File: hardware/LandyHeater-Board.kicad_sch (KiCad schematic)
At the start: 0 parts

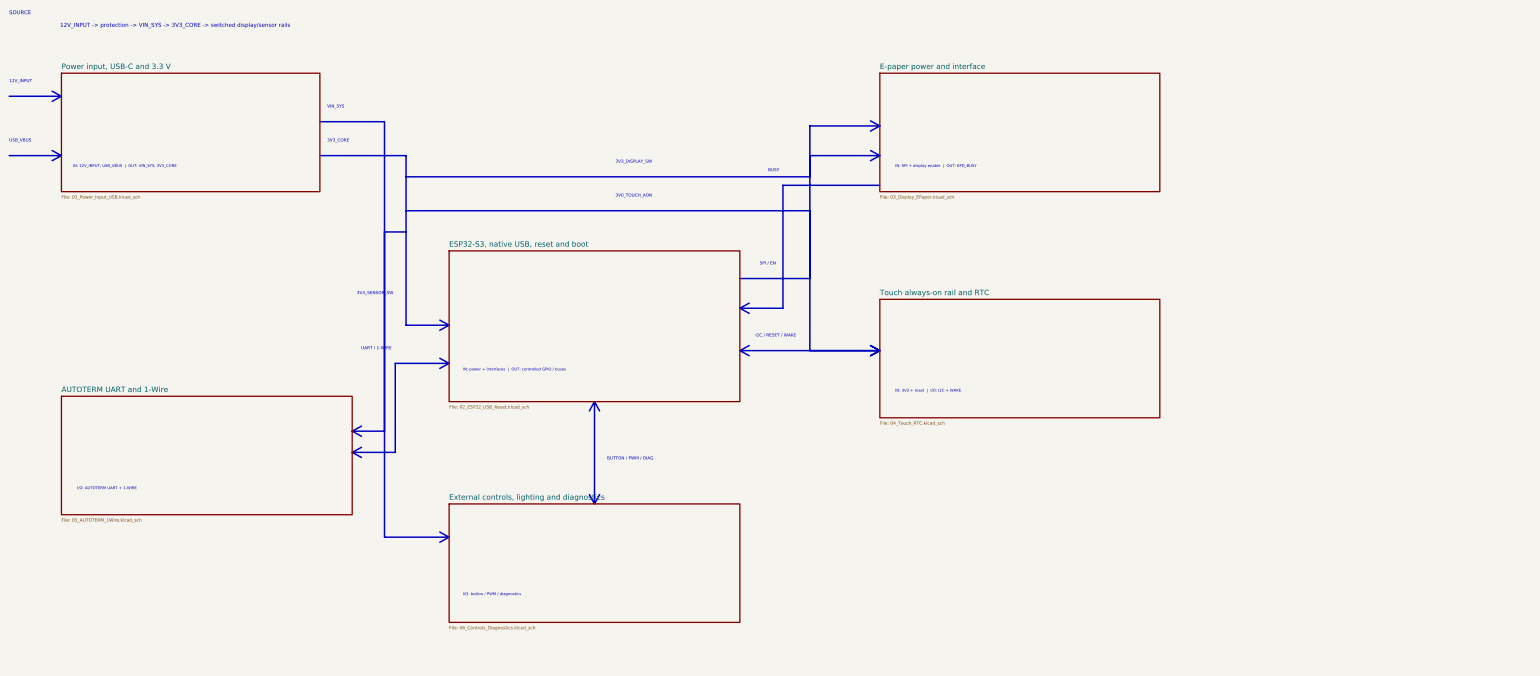
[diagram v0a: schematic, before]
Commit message: Rebuild Rev A schematic from a single verified circuit definition
- Requirements list extracted from spec v1.6 (docs/Anforderungsliste_RevA.md)
- New canonical circuit in scripts/rebuild/design.py with LCSC numbers
  (all stock-checked 2026-10-12) and generated 6-sheet KiCad schematic
- Power path kept on TI's automotive reference (LM74720-Q1 Fig. 9-1) with
  hold-up capacitor; buck moved to LMR33630C (2.1 MHz) for availability
- Fixes found during datasheet re-check: TPD2EUSB30 pinout, TPS25947 EN
  overvoltage and phantom EPAD, mirrored RV-3028 footprint, Good Display
  VSL capacitor, AL8861 VSET default, missing AUTOTERM_5V ESD, LED wire
  short-circuit protection
- ERC 0 violations; exported netlist matches the definition on all 668 pins

Co-Authored-By: Claude Opus 5.5 <noreply@anthropic.com>
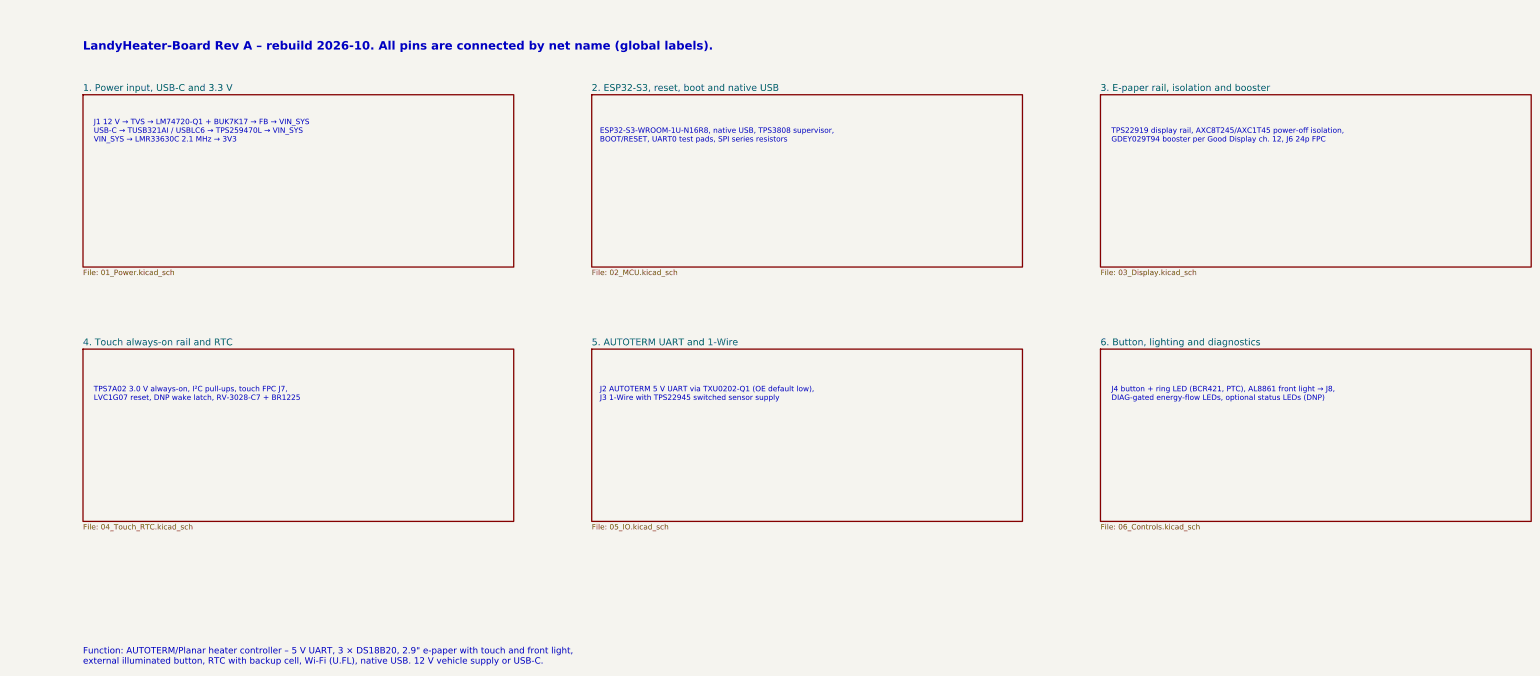
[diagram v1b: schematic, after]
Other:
- removed sheet AUTOTERM UART and 1-Wire
- removed sheet E-paper power and interface
- removed sheet ESP32-S3, native USB, reset and boot
- removed sheet External controls, lighting and diagnostics
- removed sheet Power input, USB-C and 3.3 V
- removed sheet Touch always-on rail and RTC
- added sheet 1. Power input, USB-C and 3.3 V (01_Power.kicad_sch)
- added sheet 2. ESP32-S3, reset, boot and native USB (02_MCU.kicad_sch)
- added sheet 3. E-paper rail, isolation and booster (03_Display.kicad_sch)
- added sheet 4. Touch always-on rail and RTC (04_Touch_RTC.kicad_sch)
- added sheet 5. AUTOTERM UART and 1-Wire (05_IO.kicad_sch)
- added sheet 6. Button, lighting and diagnostics (06_Controls.kicad_sch)
- note added: "ESP32-S3-WROOM-1U-N16R8, native USB, TPS3808 supervisor, BOOT/RESET, UART0 test pads, SPI series resistors"
- note added: "Function: AUTOTERM/Planar heater controller – 5 V UART, 3 × DS18B20, 2.9" e-paper with touch and front light, external illuminated button, RTC with backup cell, Wi-Fi (U.FL), native USB. 12 V vehicle supply or USB-C."
- note added: "J1 12 V → TVS → LM74720-Q1 + BUK7K17 → FB → VIN_SYS USB-C → TUSB321AI / USBLC6 → TPS259470L → VIN_SYS VIN_SYS → LMR33630C 2.1 MHz → 3V3"
- note added: "J2 AUTOTERM 5 V UART via TXU0202-Q1 (OE default low), J3 1-Wire with TPS22945 switched sensor supply"
- note added: "J4 button + ring LED (BCR421, PTC), AL8861 front light → J8, DIAG-gated energy-flow LEDs, optional status LEDs (DNP)"
- note added: "LandyHeater-Board Rev A – rebuild 2026-10. All pins are connected by net name (global labels)."
- note added: "TPS22919 display rail, AXC8T245/AXC1T45 power-off isolation, GDEY029T94 booster per Good Display ch. 12, J6 24p FPC"
- note added: "TPS7A02 3.0 V always-on, I²C pull-ups, touch FPC J7, LVC1G07 reset, DNP wake latch, RV-3028-C7 + BR1225"
- note removed: "12V_INPUT"
- note removed: "12V_INPUT -> protection -> VIN_SYS -> 3V3_CORE -> switched display/sensor rails"
- note removed: "3V0_TOUCH_AON"
- note removed: "3V3_CORE"
- note removed: "3V3_DISPLAY_SW"
- note removed: "3V3_SENSOR_SW"
- note removed: "BUSY"
- note removed: "BUTTON / PWM / DIAG"
- note removed: "I/O: AUTOTERM UART + 1-WIRE"
- note removed: "I/O: button / PWM / diagnostics"
- note removed: "I2C / RESET / WAKE"
- note removed: "IN: 12V_INPUT, USB_VBUS | OUT: VIN_SYS, 3V3_CORE"
- note removed: "IN: 3V3 + reset | I/O: I2C + WAKE"
- note removed: "IN: SPI + display enable | OUT: EPD_BUSY"
- note removed: "IN: power + interfaces | OUT: controlled GPIO / buses"
- note removed: "SOURCE"
- note removed: "SPI / EN"
- note removed: "UART / 1-WIRE"
- note removed: "USB_VBUS"
- note removed: "VIN_SYS"
- title: Landy Heater Controller - System Architecture -> LandyHeater-Board Rev A – Overview
